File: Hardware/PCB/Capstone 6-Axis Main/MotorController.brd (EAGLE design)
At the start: 60.3 x 60.3 mm, 56 parts, among them CON3 TI-JTAG-CTI-20, J1 768250004CON_768250004_MOL, J2 768250004CON_768250004_MOL, J3 MF-CON-2.54mm-01x03, J4 MF-CON-2.54mm-01x03, J5 MF-CON-2.54mm-01x03, J6 MF-CON-2.54mm-01x03, J7 MF-CON-2.54mm-01x03, J8 MF-CON-2.54mm-01x04, Q2 20MHz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

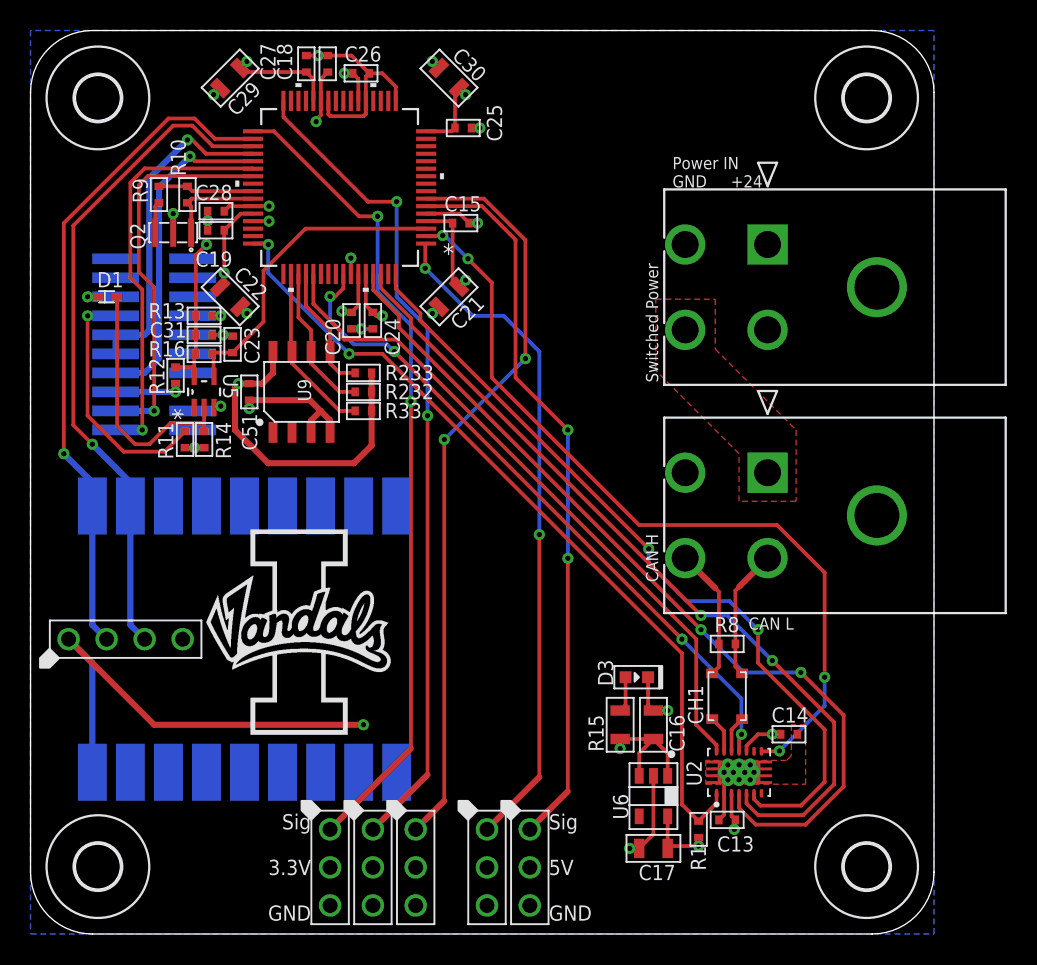
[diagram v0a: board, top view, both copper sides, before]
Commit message: Updated PCBs and added custom libraries
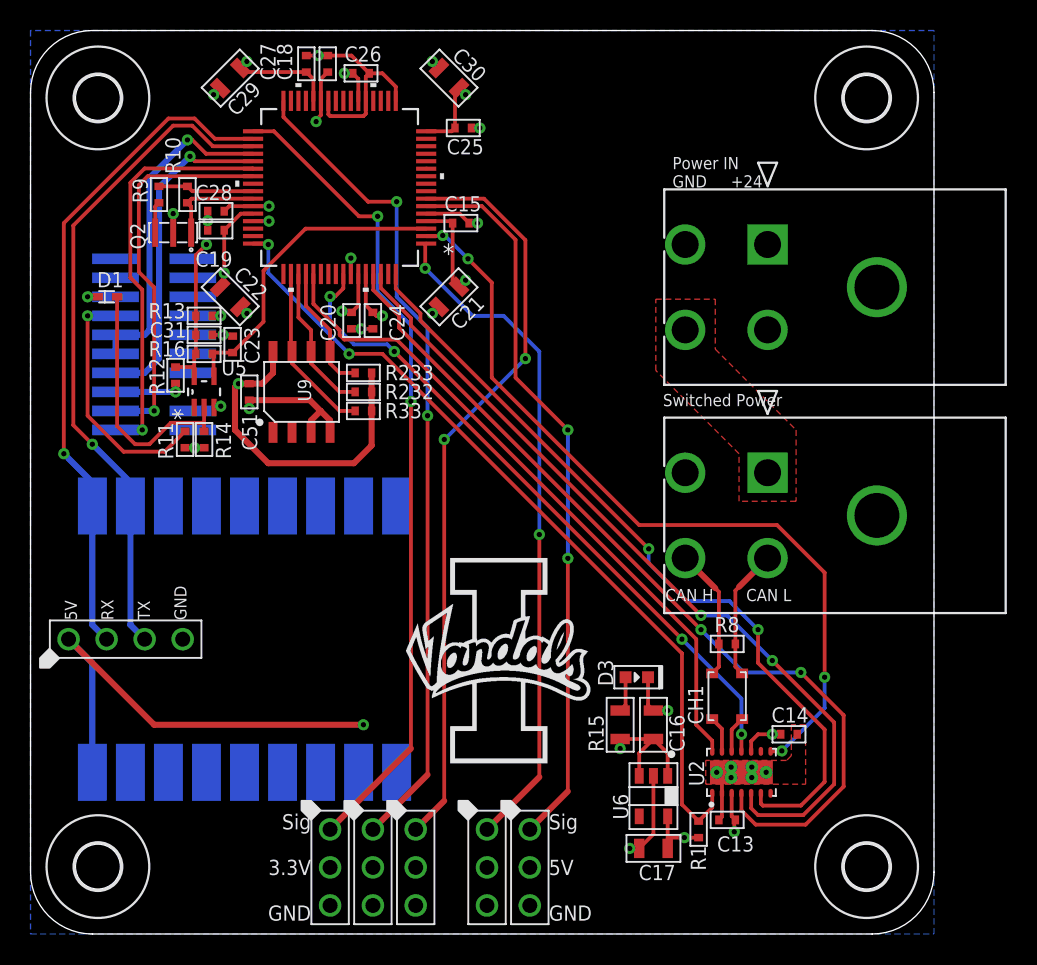
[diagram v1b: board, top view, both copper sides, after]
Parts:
- moved U2 0.16 mm to (47.5, 10.8)
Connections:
- net GND: no longer U2.15_10, U2.15_11, U2.15_12, U2.15_15, U2.15_16, U2.15_17, U2.15_21, U2.15_22, U2.15_23, U2.15_7, U2.15_8, U2.15_9
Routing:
- net GND: track 56.4 -> 50.9 mm
- net +3V3: track 76.3 -> 75.0 mm
- net MCU_SCLK: track 54.0 -> 53.5 mm
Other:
- board text added: "5V RX TX GND"
